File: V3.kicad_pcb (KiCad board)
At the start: 2 copper layers, 134.6 x 80 mm, 172 parts, among them IC1 MCP4451-103E_ST, IC2 MCP4451-103E_ST, IC3 MCP4451-103E_ST, IC4 MCP4451-103E_ST, IC5 MCP4451-103E_ST, IC6 MCP4451-103E_ST, U10 PAM8403, U11 PAM8403, U12 PAM8403, U13 PAM8403, U2 PAM8403, U3 PAM8403, U4 PAM8403, U5 PAM8403, U6 PAM8403, U7 PAM8403, U8 PAM8403, U9 PAM8403

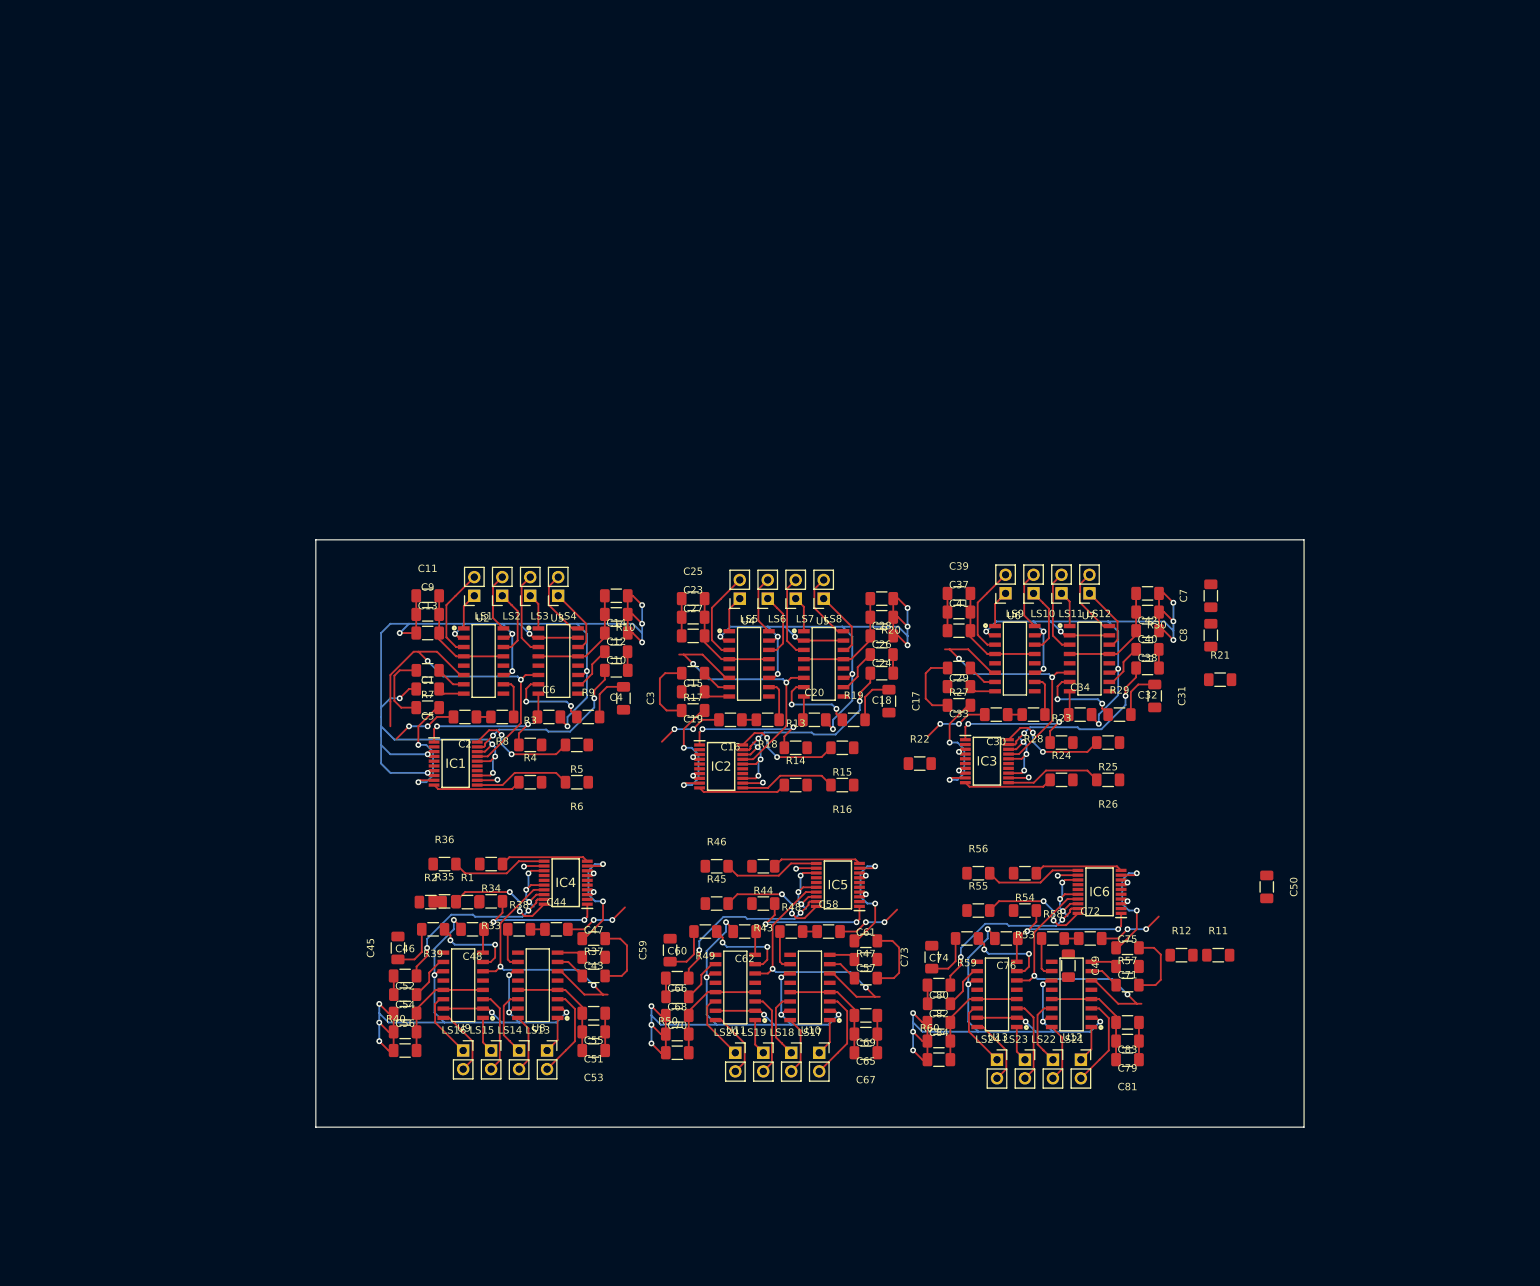
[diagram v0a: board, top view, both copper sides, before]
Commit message: Some progress before reverting to 3/3 i2c line
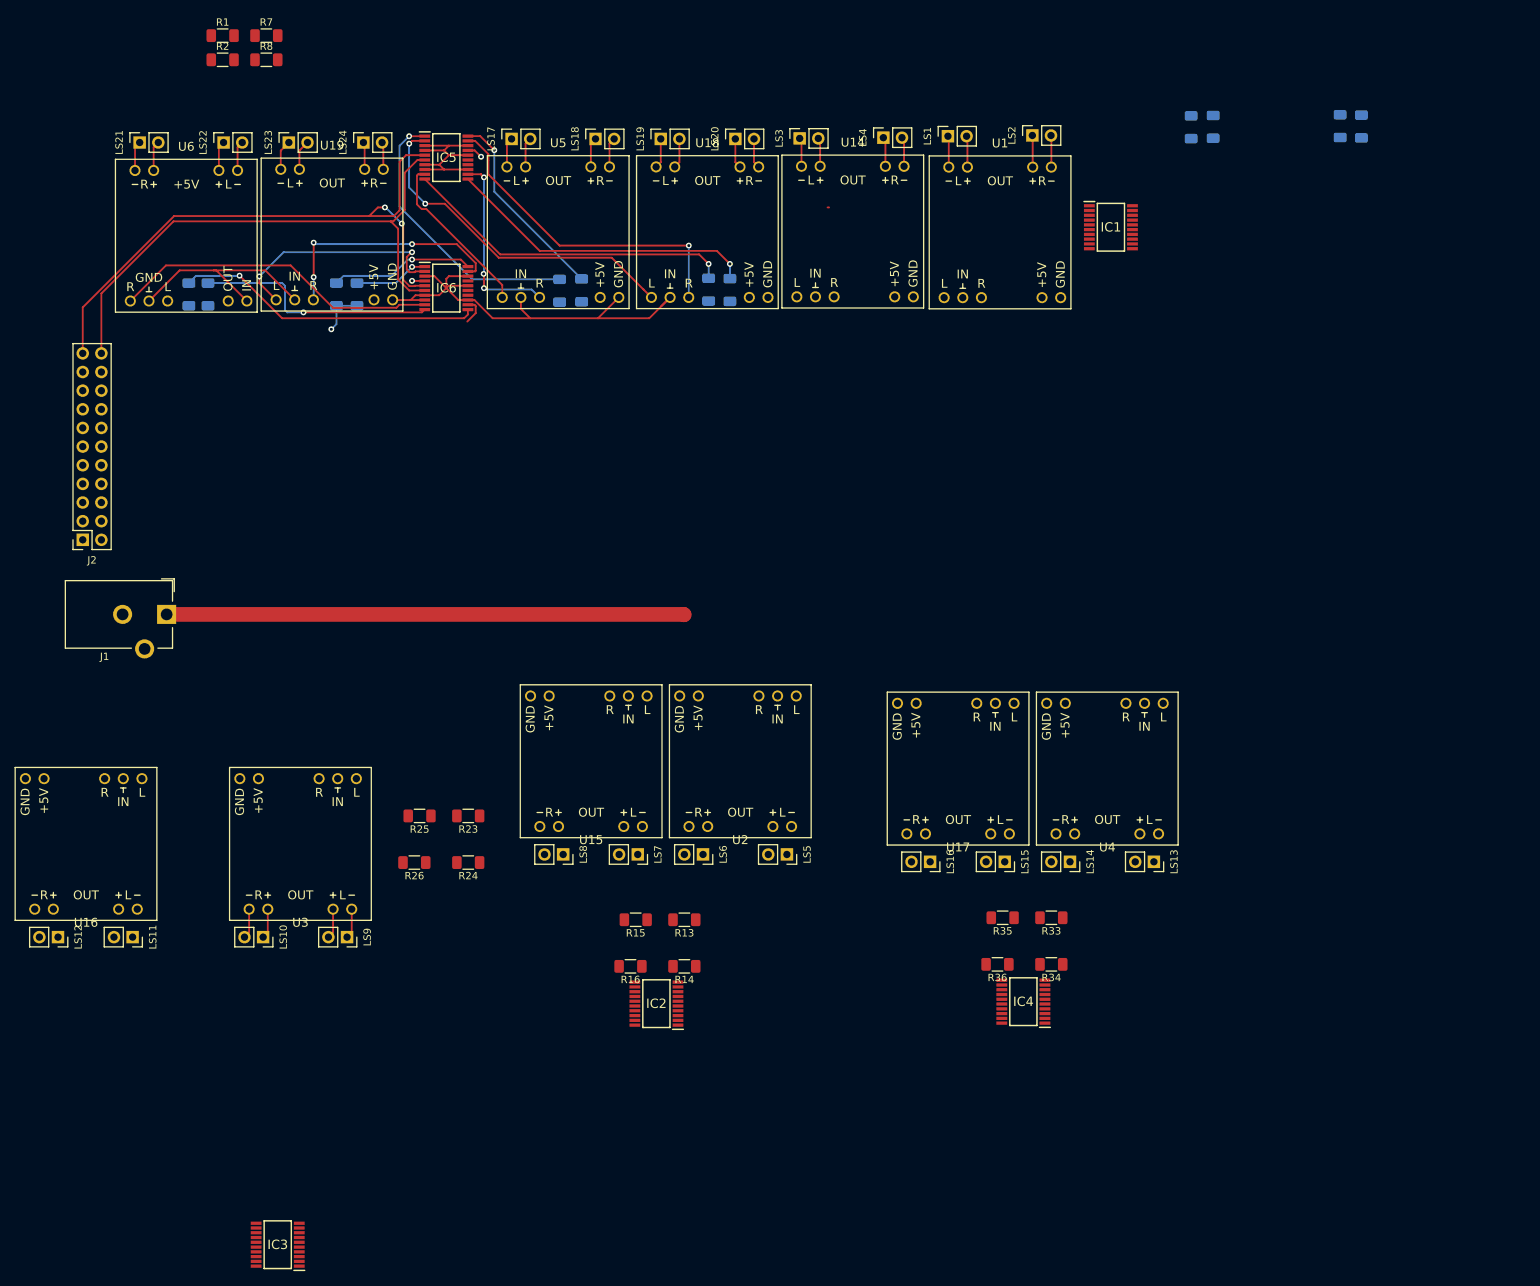
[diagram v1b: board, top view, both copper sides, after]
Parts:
- removed C1, C15, C16, C17, C18, C2, C29, C3, C30, C31, C32, C4, C43, C44, C45, C46, C57, C58, C59, C60, C71, C72, C73, C74: 0.47uF, SMD Capacitor:C_1206_3216Metric_Pad1.33x1.80mm_HandSolder
- removed C10, C13, C14, C23, C24, C27, C28, C37, C38, C41, C42, C49, C50, C51, C52, C55, C56, C65, C66, C69, C7, C70, C79, C8, C80, C83, C84, C9: 1uF, SMD Capacitor:C_1206_3216Metric_Pad1.33x1.80mm_HandSolder
- removed C11, C12, C25, C26, C39, C40, C53, C54, C67, C68, C81, C82: 470uF, SMD Capacitor:C_1206_3216Metric_Pad1.33x1.80mm_HandSolder
- removed C19, C20, C33, C34, C47, C48, C5, C6, C61, C62, C75, C76: 0.1uF, SMD Capacitor:C_1206_3216Metric_Pad1.33x1.80mm_HandSolder
- removed R10, R17, R18, R19, R20, R27, R28, R29, R30, R37, R38, R39, R40, R47, R48, R49, R50, R57, R58, R59, R60, R9: 10000, SMD Resistor:R_1206_3216Metric_Pad1.30x1.75mm_HandSolder
- removed R11, R12, R21, R22: 2200, SMD Resistor:R_1206_3216Metric_Pad1.30x1.75mm_HandSolder
- removed U10, U11, U12, U13, U7, U8, U9: PAM8403, PAM8403:SOIC127P605X150-16N
- added J1: Barrel_Jack, Barrel Jack:BarrelJack_CUI_PJ-102AH_Horizontal, F.Cu at (64.8, 66.0)
- added J2: Conn_01x22_Female, Pin Socket 2.54mm:PinSocket_2x11_P2.54mm_Vertical, F.Cu at (53.3, 55.9)
- added U1: AMPLIFIER-PAM8403, DIY modules:AMPLIFIER-PAM8403, F.Cu at (178.3, 14.0)
- added U14: AMPLIFIER-PAM8403, DIY modules:AMPLIFIER-PAM8403, F.Cu at (158.2, 13.9)
- added U15: AMPLIFIER-PAM8403, DIY modules:AMPLIFIER-PAM8403, F.Cu at (122.6, 86.0)
- added U16: AMPLIFIER-PAM8403, DIY modules:AMPLIFIER-PAM8403, F.Cu at (53.8, 97.3)
- added U17: AMPLIFIER-PAM8403, DIY modules:AMPLIFIER-PAM8403, F.Cu at (172.6, 87.0)
- added U18: AMPLIFIER-PAM8403, DIY modules:AMPLIFIER-PAM8403, F.Cu at (138.4, 14.0)
- added U19: AMPLIFIER-PAM8403, DIY modules:AMPLIFIER-PAM8403, F.Cu at (87.3, 14.3)
- R3, R4, R43, R44, R45, R46, R5, R53, R54, R55, R56, R6: moved to B.Cu
- R7, R8: value 10000 -> 2200
- U2, U3, U4, U5, U6: value PAM8403 -> AMPLIFIER-PAM8403; footprint PAM8403:SOIC127P605X150-16N -> DIY modules:AMPLIFIER-PAM8403
- moved LS21 179.0 mm to (61.1, 1.76), turned to 90 degrees
- moved LS22 168.4 mm to (72.5, 1.76), turned to 90 degrees
- moved LS23 160.2 mm to (81.4, 1.76), turned to 90 degrees
- moved LS24 151.9 mm to (91.6, 1.76), turned to 90 degrees
- moved LS12 148.1 mm to (50.0, 110.0), turned to 270 degrees
- moved R4 142.0 mm to (224.6, -0.47), turned to 270 degrees
- moved R6 139.3 mm to (227.5, -0.42), turned to 90 degrees
- moved R54 136.4 mm to (70.4, 22.4), turned to 270 degrees
- moved LS11 134.9 mm to (60.1, 110.0), turned to 270 degrees
- moved R56 133.3 mm to (67.8, 22.4), turned to 90 degrees
- moved LS17 131.3 mm to (111.8, 1.27), turned to 90 degrees
- moved LS18 127.3 mm to (123.2, 1.27), turned to 90 degrees
- moved U6 126.7 mm to (67.4, 14.5)
- moved LS19 125.3 mm to (132.1, 1.27), turned to 90 degrees
- moved LS20 124.5 mm to (142.2, 1.27), turned to 90 degrees
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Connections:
- IC1 pad 13: TeensyGND -> GND
- IC1 pad 14: Net-(IC1-Pad14) -> (no net)
- IC1 pad 15: Net-(IC1-Pad15) -> (no net)
- IC1 pad 16: TeensyGND -> GND
- IC1 pad 18: TeensyGND -> GND
- IC1 pad 3: TeensyGND -> GND
- IC1 pad 4: TeensyGND -> GND
- IC1 pad 7: TeensyGND -> GND
- IC1 pad 8: TeensyGND -> GND
- IC2 pad 12: Net-(C16-Pad2) -> Net-(IC2-Pad12)
- IC2 pad 13: TeensyGND -> GND
- IC2 pad 14: Net-(IC2-Pad14) -> (no net)
- IC2 pad 15: Net-(IC2-Pad15) -> (no net)
- IC2 pad 16: TeensyGND -> GND
- IC2 pad 18: TeensyGND -> GND
- IC2 pad 3: TeensyGND -> GND
- IC2 pad 4: TeensyGND -> TeensyVVD
- IC2 pad 7: TeensyGND -> GND
- IC2 pad 8: TeensyGND -> GND
- IC2 pad 9: Net-(C15-Pad2) -> Net-(IC2-Pad9)
- IC3 pad 12: Net-(C30-Pad2) -> Net-(IC3-Pad12)
- IC3 pad 13: TeensyGND -> GND
- IC3 pad 14: Net-(IC3-Pad14) -> (no net)
- IC3 pad 15: Net-(IC3-Pad15) -> (no net)
- IC3 pad 16: TeensyGND -> TeensyVVD
- IC3 pad 18: TeensyGND -> GND
- IC3 pad 3: TeensyGND -> GND
- IC3 pad 4: TeensyGND -> GND
- IC3 pad 7: TeensyGND -> GND
- IC3 pad 8: TeensyGND -> GND
- IC3 pad 9: Net-(C29-Pad2) -> Net-(IC3-Pad9)
- IC4 pad 12: Net-(C44-Pad2) -> Net-(IC4-Pad12)
- IC4 pad 13: TeensyGND -> GND
- IC4 pad 14: Net-(IC4-Pad14) -> (no net)
- IC4 pad 15: Net-(IC4-Pad15) -> (no net)
- IC4 pad 16: TeensyGND -> TeensyVVD
- IC4 pad 18: TeensyGND -> GND
- IC4 pad 3: TeensyGND -> GND
- IC4 pad 4: TeensyGND -> TeensyVVD
- IC4 pad 7: TeensyGND -> GND
- IC4 pad 8: TeensyGND -> GND
- IC4 pad 9: Net-(C43-Pad2) -> Net-(IC4-Pad9)
- IC5 pad 12: Net-(C58-Pad2) -> Net-(IC5-Pad12)
- IC5 pad 13: TeensyGND -> GND
- IC5 pad 14: Net-(IC5-Pad14) -> (no net)
- IC5 pad 15: Net-(IC5-Pad15) -> (no net)
- IC5 pad 16: TeensyGND -> GND
- IC5 pad 18: TeensyGND -> GND
- IC5 pad 3: TeensyGND -> GND
- IC5 pad 4: TeensyGND -> GND
- IC5 pad 7: TeensyGND -> GND
- IC5 pad 8: TeensyGND -> GND
- IC5 pad 9: Net-(C57-Pad2) -> Net-(IC5-Pad9)
- IC6 pad 12: Net-(C72-Pad2) -> Net-(IC6-Pad12)
- IC6 pad 13: TeensyGND -> GND
- IC6 pad 14: Net-(IC6-Pad14) -> (no net)
- IC6 pad 15: Net-(IC6-Pad15) -> (no net)
- IC6 pad 16: TeensyGND -> GND
- IC6 pad 18: TeensyGND -> GND
- IC6 pad 3: TeensyGND -> GND
- IC6 pad 4: TeensyGND -> TeensyVVD
- IC6 pad 7: TeensyGND -> GND
- IC6 pad 8: TeensyGND -> GND
- IC6 pad 9: Net-(C71-Pad2) -> Net-(IC6-Pad9)
- R7 pad 1: Net-(R7-Pad1) -> SCL1
- R7 pad 2: Net-(C1-Pad1) -> TeensyVDD
- R8 pad 1: Net-(R8-Pad1) -> SDA1
- R8 pad 2: Net-(C2-Pad1) -> TeensyVDD
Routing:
- net TeensyGND: track 686.5 -> 0.00 mm, vias 86 -> 0
- net TeensyVDD: track 256.1 -> 2.15 mm, vias 12 -> 1
- net GND: track 0.00 -> 117.1 mm
- net SCL1: track 0.00 -> 82.2 mm, vias 0 -> 2
- net SDA1: track 0.00 -> 75.3 mm
- net VDD: track 0.00 -> 70.5 mm
- net Net-(IC5-Pad2): track 0.00 -> 47.5 mm, vias 0 -> 2
- net Net-(IC6-Pad9): track 0.00 -> 44.7 mm
- net Net-(IC5-Pad10): track 12.2 -> 45.4 mm, vias 0 -> 1
- net Net-(IC6-Pad2): track 0.00 -> 31.7 mm, vias 0 -> 2
- net Net-(IC5-Pad11): track 13.2 -> 42.5 mm, vias 0 -> 1
- net Net-(IC6-Pad11): track 13.2 -> 42.3 mm, vias 0 -> 1
- net Net-(IC5-Pad12): track 0.00 -> 25.6 mm, vias 0 -> 3
- net Net-(IC3-Pad19): track 24.2 -> 0.00 mm, vias 2 -> 0
- net Net-(IC1-Pad19): track 24.2 -> 0.00 mm, vias 2 -> 0
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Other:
- board outline removed

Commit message: Finalize PCB v0
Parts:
- removed R33, R34, R35, R36, R43, R44, R45, R46, R53, R54, R55, R56: 51000, SMD Resistor:R_1206_3216Metric_Pad1.30x1.75mm_HandSolder
- removed U14, U15, U16, U17, U18, U19: AMPLIFIER-PAM8403, DIY modules:AMPLIFIER-PAM8403
- added R10: 51000, SMD Resistor:R_1206_3216Metric_Pad1.30x1.75mm_HandSolder, B.Cu at (119.1, 79.6)
- added R11: 51000, SMD Resistor:R_1206_3216Metric_Pad1.30x1.75mm_HandSolder, B.Cu at (136.6, 79.3)
- added R12: 51000, SMD Resistor:R_1206_3216Metric_Pad1.30x1.75mm_HandSolder, B.Cu at (116.6, 79.6)
- added R17: 51000, SMD Resistor:R_1206_3216Metric_Pad1.30x1.75mm_HandSolder, B.Cu at (181.3, 113.0)
- added R18: 51000, SMD Resistor:R_1206_3216Metric_Pad1.30x1.75mm_HandSolder, B.Cu at (163.3, 113.0)
- added R19: 51000, SMD Resistor:R_1206_3216Metric_Pad1.30x1.75mm_HandSolder, B.Cu at (183.8, 113.0)
- added R20: 51000, SMD Resistor:R_1206_3216Metric_Pad1.30x1.75mm_HandSolder, B.Cu at (160.6, 113.0)
- added R21: 51000, SMD Resistor:R_1206_3216Metric_Pad1.30x1.75mm_HandSolder, B.Cu at (135.6, 112.8)
- added R22: 51000, SMD Resistor:R_1206_3216Metric_Pad1.30x1.75mm_HandSolder, B.Cu at (114.7, 112.8)
- added R27: 51000, SMD Resistor:R_1206_3216Metric_Pad1.30x1.75mm_HandSolder, B.Cu at (233.1, 113.0)
- added R28: 51000, SMD Resistor:R_1206_3216Metric_Pad1.30x1.75mm_HandSolder, B.Cu at (210.0, 113.0)
- added R9: 51000, SMD Resistor:R_1206_3216Metric_Pad1.30x1.75mm_HandSolder, B.Cu at (139.1, 79.3)
- added U10: AMPLIFIER-PAM8403, DIY modules:AMPLIFIER-PAM8403, F.Cu at (135.6, 120.7)
- added U11: AMPLIFIER-PAM8403, DIY modules:AMPLIFIER-PAM8403, F.Cu at (212.6, 120.8)
- added U12: AMPLIFIER-PAM8403, DIY modules:AMPLIFIER-PAM8403, F.Cu at (233.0, 120.8)
- added U7: AMPLIFIER-PAM8403, DIY modules:AMPLIFIER-PAM8403, F.Cu at (163.7, 120.9)
- added U8: AMPLIFIER-PAM8403, DIY modules:AMPLIFIER-PAM8403, F.Cu at (184.1, 120.9)
- added U9: AMPLIFIER-PAM8403, DIY modules:AMPLIFIER-PAM8403, F.Cu at (115.1, 120.7)
- R13, R14, R15, R16, R23, R24, R25, R26: moved to B.Cu
- R3, R4: value 51000 -> 2200; moved to F.Cu
- R7, R8: value 2200 -> 51000; moved to B.Cu
- moved LS21 223.2 mm to (240.0, 135.1), turned to 270 degrees
- moved LS22 205.3 mm to (228.6, 135.1), turned to 270 degrees
- moved LS12 196.8 mm to (240.1, 59.1), turned to 90 degrees
- moved LS23 192.0 mm to (219.6, 135.1), turned to 270 degrees
- moved LS24 177.1 mm to (208.2, 135.1), turned to 270 degrees
- moved LS11 176.1 mm to (228.7, 59.1), turned to 90 degrees
- moved R4 167.3 mm to (93.8, 103.8)
- moved U6 159.1 mm to (215.2, 73.4)
- moved LS10 150.6 mm to (219.7, 59.1), turned to 90 degrees
- moved R3 147.9 mm to (93.8, 98.0)
- moved IC6 142.7 mm to (198.2, 127.7), turned to 180 degrees
- moved R7 142.2 mm to (186.7, 79.3), turned to 90 degrees
- moved IC3 141.3 mm to (200.7, 78.6), turned to 0 degrees
- moved LS20 137.4 mm to (110.7, 135.0), turned to 270 degrees
- moved LS17 137.2 mm to (142.6, 135.0), turned to 270 degrees
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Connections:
- IC2 pad 4: TeensyVVD -> TeensyVDD
- IC3 pad 16: TeensyVVD -> TeensyVDD
- IC4 pad 16: TeensyVVD -> GND
- IC4 pad 4: TeensyVVD -> GND
- IC4 pad 5: SCL0 -> SCL1
- IC4 pad 6: SDA0 -> SDA1
- IC5 pad 4: GND -> TeensyVDD
- IC6 pad 16: GND -> TeensyVDD
- IC6 pad 4: TeensyVVD -> GND
- R13 pad 1: Net-(IC2-Pad1) -> Net-(IC3-Pad1)
- R13 pad 2: FREQ8 -> FREQ10
- R14 pad 1: Net-(IC2-Pad10) -> Net-(IC3-Pad10)
- R14 pad 2: FREQ6 -> FREQ9
- R15 pad 1: FREQ7 -> FREQ10
- R15 pad 2: Net-(IC2-Pad20) -> Net-(IC3-Pad20)
- R16 pad 1: FREQ5 -> FREQ9
- R16 pad 2: Net-(IC2-Pad11) -> Net-(IC3-Pad11)
- R23 pad 1: Net-(IC3-Pad1) -> FREQ14
- R23 pad 2: FREQ10 -> Net-(IC5-Pad20)
- R24 pad 1: Net-(IC3-Pad10) -> FREQ13
- R24 pad 2: FREQ9 -> Net-(IC5-Pad11)
- R25 pad 1: FREQ10 -> Net-(IC6-Pad1)
- R25 pad 2: Net-(IC3-Pad20) -> FREQ16
- R26 pad 1: FREQ9 -> Net-(IC6-Pad10)
- R26 pad 2: Net-(IC3-Pad11) -> FREQ15
- R3 pad 1: Net-(IC1-Pad1) -> SCL1
- R3 pad 2: FREQ4 -> TeensyVDD
- R4 pad 1: Net-(IC1-Pad10) -> SDA1
- R4 pad 2: FREQ2 -> TeensyVDD
- R5 pad 1: FREQ3 -> Net-(IC1-Pad1)
- R5 pad 2: Net-(IC1-Pad20) -> FREQ4
- R6 pad 1: FREQ1 -> Net-(IC1-Pad10)
- R6 pad 2: Net-(IC1-Pad11) -> FREQ2
- R7 pad 1: SCL1 -> FREQ3
- R7 pad 2: TeensyVDD -> Net-(IC1-Pad20)
- R8 pad 1: SDA1 -> FREQ1
- R8 pad 2: TeensyVDD -> Net-(IC1-Pad11)
- U1 pad IN.L: Net-(IC1-Pad9) -> Net-(IC1-Pad2)
- U1 pad IN.R: Net-(IC1-Pad12) -> Net-(IC1-Pad19)
- U1 pad OUT.L+: Net-(LS1-Pad2) -> Net-(LS3-Pad2)
- U1 pad OUT.L-: Net-(LS1-Pad1) -> Net-(LS3-Pad1)
- U1 pad OUT.R+: Net-(LS2-Pad1) -> Net-(LS4-Pad1)
- U1 pad OUT.R-: Net-(LS2-Pad2) -> Net-(LS4-Pad2)
- U2 pad IN.L: Net-(IC2-Pad9) -> Net-(IC1-Pad9)
- U2 pad IN.R: Net-(IC2-Pad12) -> Net-(IC1-Pad12)
- U2 pad OUT.L+: Net-(LS5-Pad2) -> Net-(LS1-Pad2)
- U2 pad OUT.L-: Net-(LS5-Pad1) -> Net-(LS1-Pad1)
- U2 pad OUT.R+: Net-(LS6-Pad1) -> Net-(LS2-Pad1)
- U2 pad OUT.R-: Net-(LS6-Pad2) -> Net-(LS2-Pad2)
- U3 pad IN.L: Net-(IC3-Pad9) -> Net-(IC2-Pad2)
- U3 pad IN.R: Net-(IC3-Pad12) -> Net-(IC2-Pad19)
- U3 pad OUT.L+: Net-(LS9-Pad2) -> Net-(LS7-Pad2)
- U3 pad OUT.L-: Net-(LS9-Pad1) -> Net-(LS7-Pad1)
- U3 pad OUT.R+: Net-(LS10-Pad1) -> Net-(LS8-Pad1)
- U3 pad OUT.R-: Net-(LS10-Pad2) -> Net-(LS8-Pad2)
- U4 pad IN.L: Net-(IC4-Pad9) -> Net-(IC2-Pad9)
- U4 pad IN.R: Net-(IC4-Pad12) -> Net-(IC2-Pad12)
- U4 pad OUT.L+: Net-(LS13-Pad2) -> Net-(LS5-Pad2)
- U4 pad OUT.L-: Net-(LS13-Pad1) -> Net-(LS5-Pad1)
- U4 pad OUT.R+: Net-(LS14-Pad1) -> Net-(LS6-Pad1)
- U4 pad OUT.R-: Net-(LS14-Pad2) -> Net-(LS6-Pad2)
- U5 pad IN.L: Net-(IC5-Pad9) -> Net-(IC3-Pad2)
- U5 pad IN.R: Net-(IC5-Pad12) -> Net-(IC3-Pad19)
- U5 pad OUT.L+: Net-(LS17-Pad2) -> Net-(LS11-Pad2)
- U5 pad OUT.L-: Net-(LS17-Pad1) -> Net-(LS11-Pad1)
- U5 pad OUT.R+: Net-(LS18-Pad1) -> Net-(LS12-Pad1)
- U5 pad OUT.R-: Net-(LS18-Pad2) -> Net-(LS12-Pad2)
- U6 pad IN.L: Net-(IC6-Pad9) -> Net-(IC3-Pad9)
- U6 pad IN.R: Net-(IC6-Pad12) -> Net-(IC3-Pad12)
- U6 pad OUT.L+: Net-(LS21-Pad2) -> Net-(LS9-Pad2)
- U6 pad OUT.L-: Net-(LS21-Pad1) -> Net-(LS9-Pad1)
- U6 pad OUT.R+: Net-(LS22-Pad1) -> Net-(LS10-Pad1)
- U6 pad OUT.R-: Net-(LS22-Pad2) -> Net-(LS10-Pad2)
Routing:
- net GND: track 117.1 -> 571.5 mm, vias 0 -> 8
- net TeensyVDD: track 2.15 -> 388.5 mm, vias 1 -> 15
- net VDD: track 70.5 -> 388.2 mm
- net SCL0: track 0.00 -> 185.7 mm, vias 0 -> 8
- net SDA0: track 0.00 -> 182.5 mm, vias 0 -> 8
- net SDA1: track 75.3 -> 249.1 mm, vias 0 -> 9
- net SCL1: track 82.2 -> 247.4 mm, vias 2 -> 7
- net FREQ10: track 0.00 -> 153.6 mm, vias 0 -> 1
- net FREQ16: track 6.29 -> 157.9 mm
- net FREQ15: track 0.00 -> 140.8 mm, vias 0 -> 1
- net FREQ9: track 0.00 -> 137.6 mm, vias 0 -> 1
- net FREQ3: track 0.00 -> 112.6 mm, vias 0 -> 1
- net FREQ4: track 0.00 -> 111.2 mm, vias 0 -> 1
- net FREQ12: track 0.00 -> 104.1 mm, vias 0 -> 1
- net FREQ1: track 0.00 -> 95.1 mm, vias 0 -> 1
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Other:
- board outline added: 164.6 x 93.3 mm

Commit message: Finalize PCB
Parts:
- added ?: , HART:hart-logo-2000-2000dpi, F.Cu at (95.4, 132.5)
- moved R2 32.4 mm to (100.4, 60.2), turned to 180 degrees
- moved R1 29.5 mm to (100.5, 57.7), turned to 180 degrees
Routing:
- net GND: track 571.5 -> 624.1 mm, vias 8 -> 6
- net SCL1: track 247.4 -> 207.7 mm
- net SDA1: track 249.1 -> 216.1 mm, vias 9 -> 8
- net SCL0: track 185.7 -> 174.4 mm
- net SDA0: track 182.5 -> 173.9 mm, vias 8 -> 10
- net TeensyVDD: track 388.5 -> 392.2 mm
- net Net-(IC4-Pad12): track 12.1 -> 10.8 mm
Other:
- board text added: "Prototype V3"
